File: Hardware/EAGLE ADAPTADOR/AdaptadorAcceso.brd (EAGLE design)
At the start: 60 x 49 mm, 9 parts

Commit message: Access Adaptation Board Correction
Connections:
- net IO18: now also J4.1; no longer J4.3
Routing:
- net IO18: track 31.7 -> 21.1 mm
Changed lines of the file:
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@@
 <layer number="14" name="Route14" color="1" fill="6" visible="no" active="no"/>
 <layer number="15" name="Route15" color="4" fill="6" visible="no" active="no"/>
-<layer number="16" name="Bottom" color="1" fill="1" visible="yes" active="yes"/>
+<layer number="16" name="Bottom" color="1" fill="1" visible="no" active="yes"/>
 <layer number="17" name="Pads" color="2" fill="1" visible="yes" active="yes"/>
 <layer number="18" name="Vias" color="2" fill="1" visible="yes" active="yes"/>
@@
 </signal>
 <signal name="IO18" class="2">
-<contactref element="J4" pad="3"/>
 <contactref element="SV1" pad="10"/>
-<wire x1="48.8328" y1="23.84199375" x2="46.10759375" y2="26.5672" width="0.5" layer="1"/>
-<wire x1="43.1" y1="15.31" x2="46.042" y2="15.31" width="0.5" layer="1"/>
-<wire x1="46.10759375" y1="26.5672" x2="33.6828" y2="26.5672" width="0.5" layer="1"/>
-<wire x1="46.042" y1="15.31" x2="48.8328" y2="18.1008" width="0.5" layer="1"/>
-<wire x1="48.8328" y1="18.1008" x2="48.8328" y2="23.84199375" width="0.5" layer="1"/>
+<wire x1="34.6828" y1="25.5672" x2="44.092275" y2="25.5672" width="0.5" layer="1"/>
 <wire x1="32.73" y1="27.52" x2="32.73" y2="29" width="0.5" layer="1"/>
-<wire x1="33.6828" y1="26.5672" x2="32.73" y2="27.52" width="0.5" layer="1"/>
+<wire x1="34.6828" y1="25.5672" x2="32.73" y2="27.52" width="0.5" layer="1"/>
+<wire x1="44.092275" y1="25.5672" x2="45.530475" y2="24.129" width="0.5" layer="1"/>
+<contactref element="J4" pad="1"/>
+<wire x1="45.530475" y1="21.695" x2="45.530475" y2="24.129" width="0.5" layer="1"/>
+<wire x1="43.1" y1="20.39" x2="44.225475" y2="20.39" width="0.5" layer="1"/>
+<wire x1="45.530475" y1="21.695" x2="44.225475" y2="20.39" width="0.5" layer="1"/>
 </signal>
 <signal name="IO40" class="2">

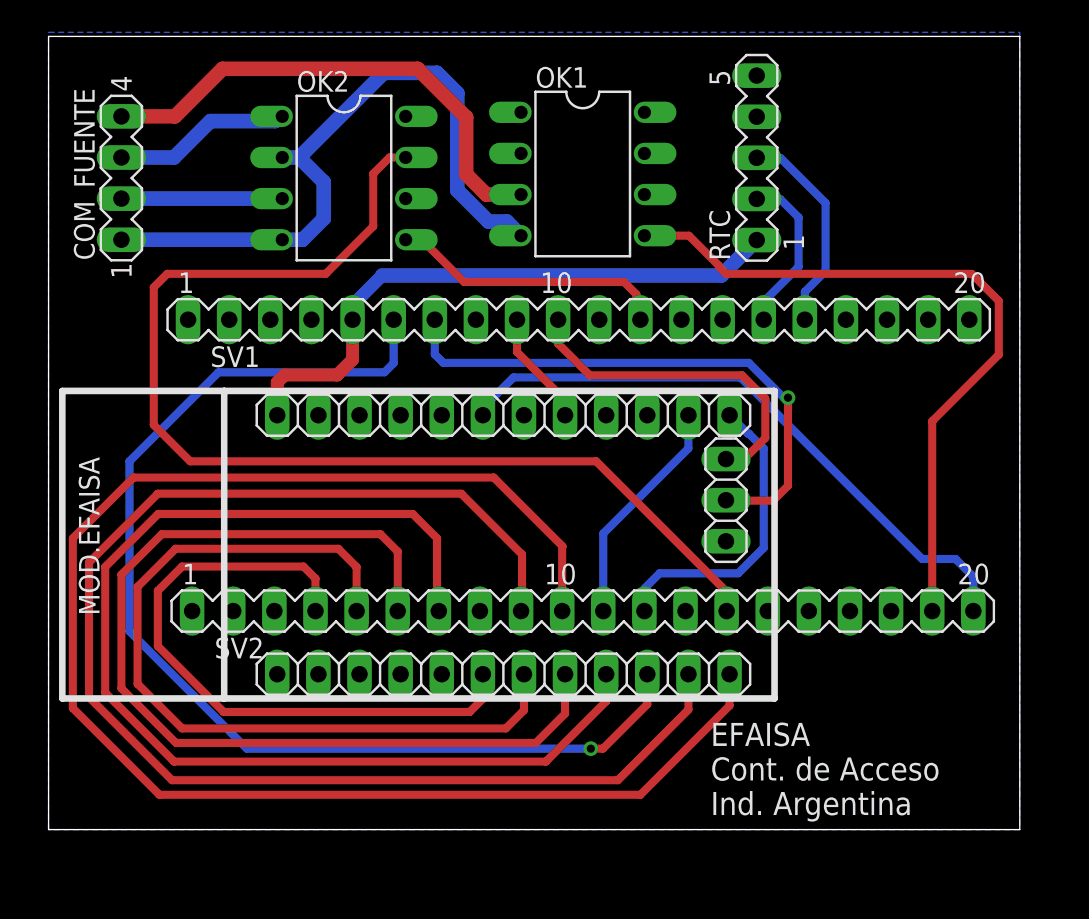
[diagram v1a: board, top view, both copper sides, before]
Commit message: Adaptation Board Modifcation, Modifed pins in main
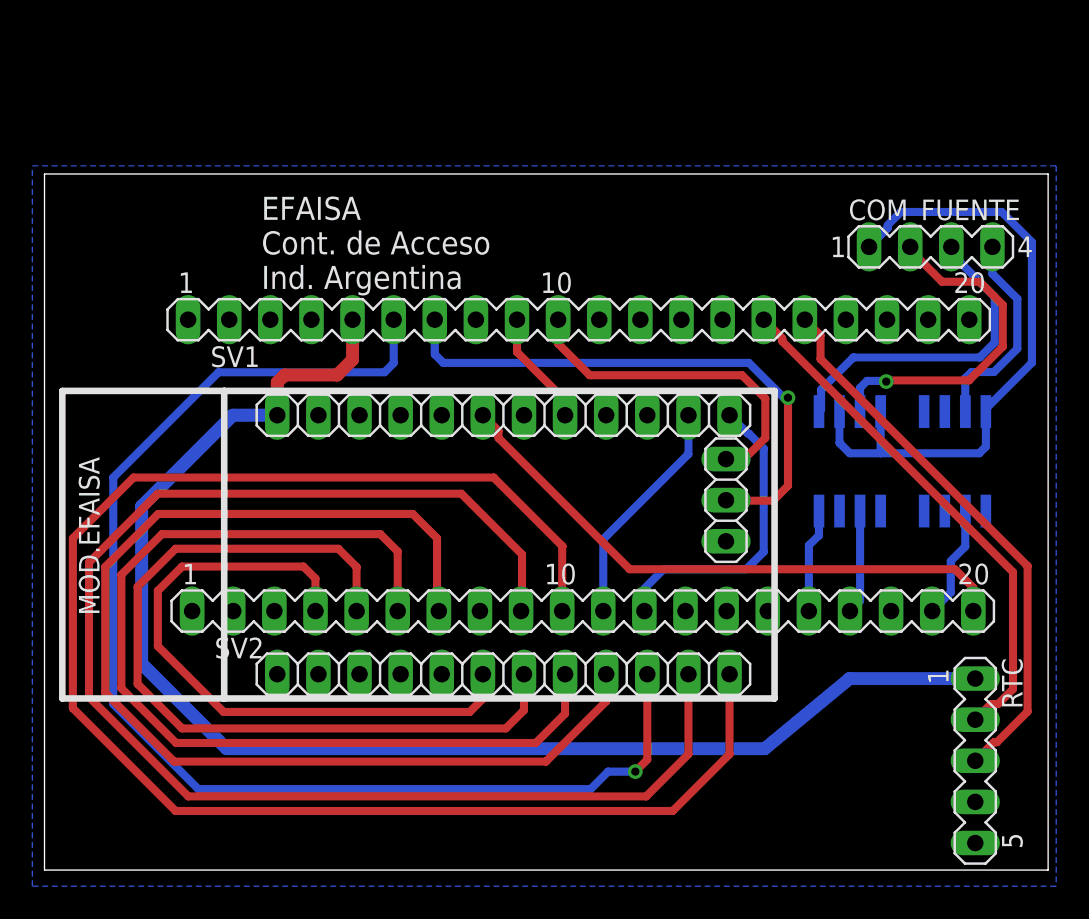
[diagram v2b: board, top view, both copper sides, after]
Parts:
- OK1, OK2: value ILD610 -> ILD205; device optocoupler:DIL08 -> optocoupler:SOIC08
- moved COM_FUENTE 50.2 mm to (55.8, 33.5), turned to 0 degrees
- moved RTC 39.6 mm to (58.5, 1.75), turned to 270 degrees
- moved OK2 35.8 mm to (50.8, 20.2), flipped to the bottom, turned to 180 degrees
- moved OK1 29.1 mm to (57.2, 20.2), flipped to the bottom, turned to 180 degrees
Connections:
- net C_OPTO1: now also OK1.6; no longer OK1.5
- net C_OPTO2: now also OK2.8, SV2.16; no longer OK2.7, SV2.14
- net C_OPTO3: now also OK2.6, SV2.17; no longer OK2.5, SV1.12
- net GNDA: now also OK1.5, OK2.5, OK2.7; no longer OK1.6, OK2.6, OK2.8
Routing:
- net C_OPTO2: track 70.1 -> 6.44 mm
- net +3V3: track 37.3 -> 85.4 mm
- net C_OPTO1: track 44.5 -> 7.02 mm
- net DATA_RTC: track 10.3 -> 32.3 mm
- net CLOCK_RTC: track 13.1 -> 34.4 mm
- net N$1: track 31.2 -> 13.0 mm
- net N$3: track 9.94 -> 21.3 mm, vias 0 -> 1
- net C_OPTO3: track 17.3 -> 6.44 mm
- net N$2: track 11.0 -> 20.4 mm
- net IO21: track 70.0 -> 78.1 mm
- net IO41: track 95.1 -> 97.7 mm
- net IO42: track 85.1 -> 87.5 mm
- net GND_FUENTE: track 42.0 -> 39.6 mm
- net IO33: track 38.7 -> 36.4 mm
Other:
- board size 60 x 49 mm -> 62 x 43 mm
